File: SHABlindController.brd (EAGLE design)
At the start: 130.5 x 22 mm, 39 parts, among them IC1 SPARKCORE, IC2 HLKPM01, IC3 RXB1, Q1 2N7002, Q2 2N7002

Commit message: Added value to fuse
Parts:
- F1: value (none) -> 250V 3A
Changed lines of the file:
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@@
 <element name="PIEZO2" library="freetronics-jon" package="PIEZO12MMWIDEPOLARISED" value="PIEZOPOLARISED" x="23" y="11" rot="MR180"/>
 <element name="IC2" library="freetronics-jon" package="HLKPM01" value="HLKPM01" x="57" y="11" rot="MR0"/>
-<element name="F1" library="freetronics-jon" package="PICOFUSE" value="" x="62" y="8.5">
+<element name="F1" library="freetronics-jon" package="PICOFUSE" value="250V 3A" x="62" y="8.5">
 <attribute name="OC_NEWARK" value="unknown" x="62" y="8.5" size="1.778" layer="27" display="off"/>
 <attribute name="MPN" value="" x="62" y="8.5" size="1.778" layer="27" display="off"/>

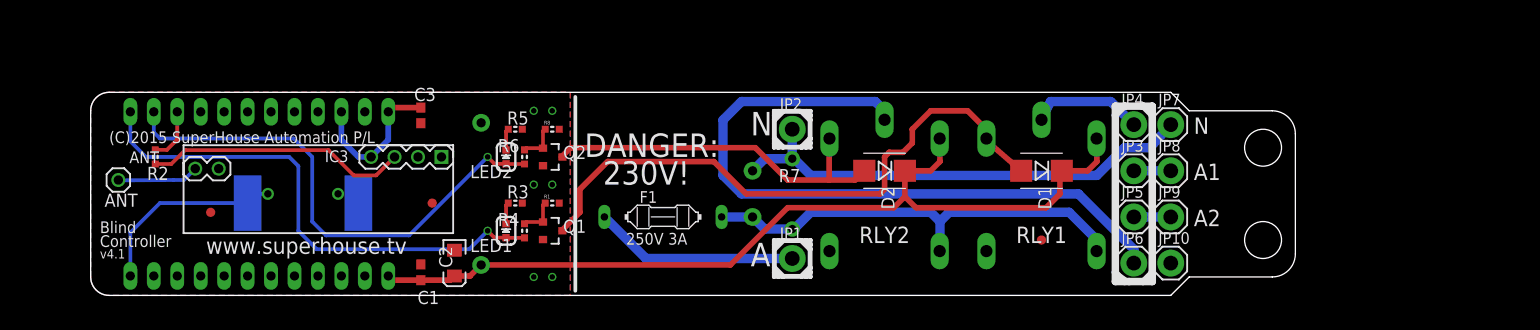
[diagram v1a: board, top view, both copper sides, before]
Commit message: Added solder-jumper to link GND and Neutral Reduced spacing between relays Increased length of fuse footprint
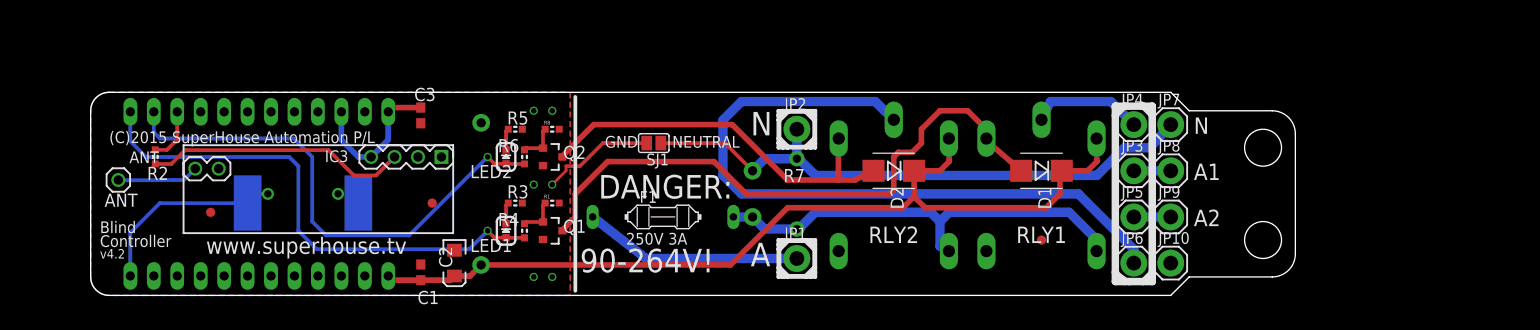
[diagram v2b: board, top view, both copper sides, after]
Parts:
- added SJ1: GND-NEUTRAL-LINK, freetronics-master-v1.1:SJ
- moved D2 1.00 mm to (87.0, 13.5)
- moved RLY2 1.00 mm to (87.0, 9.50)
- moved JP1 0.50 mm to (76.5, 4.00)
- moved JP2 0.50 mm to (76.5, 18.0)
- moved R7 0.50 mm to (76.5, 11.0)
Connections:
- net GND: now also SJ1.2
- net NEUTRAL: now also SJ1.1
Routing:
- net GND: track 0.00 -> 12.4 mm
- net NEUTRAL: track 52.4 -> 63.6 mm
- net N$3: track 40.7 -> 43.6 mm
- net N$9: track 22.2 -> 23.7 mm
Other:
- board text added: "90-264V!"
- board text added: "GND"
- board text added: "NEUTRAL"
- board text added: "v4.2"
- board text removed: "230V!"
- board text removed: "v4.1"

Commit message: Layout updates
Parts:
- removed JP10: EARTH, freetronics-master-v1.1:1X01LARGE
- removed JP3, JP8: ACTIVE1, freetronics-master-v1.1:1X01LARGE
- removed JP5, JP9: ACTIVE2, freetronics-master-v1.1:1X01LARGE
- added C4: 100nF 0603, freetronics-master-v1.1:0603
- added IC4: AH180-PL-A, freetronics-jon:TO92FLATUP
- added LED3: ROTATE/GREEN, freetronics:LED-0603
- added R10: 1K 0603, freetronics-master-v1:0603
- added R11, R9: 10K 0603, freetronics-master-v1:0603
- added R12: 10K, freetronics:0603
- added S2: 2P-JST-PTH, freetronics-jon:JST-2MM-TH-RA
- moved F1 73.5 mm to (135.5, 10.0), flipped to the bottom, turned to 90 degrees
- moved JP2 69.5 mm to (145.0, 6.00)
- moved JP1 69.2 mm to (145.0, 14.0)
- moved R7 63.0 mm to (139.5, 13.0)
- moved JP6 35.3 mm to (141.0, 25.0)
- moved JP4 33.6 mm to (146.0, 25.0)
- moved FID2 29.2 mm to (42.0, 12.0)
- moved C1 25.3 mm to (60.8, 6.50)
- moved C2 25.3 mm to (64.4, 7.50)
- moved C3 25.3 mm to (60.8, 23.5)
- moved FID3 25.3 mm to (62.0, 14.0)
- moved IC1 25.3 mm to (42.0, 15.0)
- moved IC2 25.3 mm to (82.0, 15.0)
- moved IC3 25.3 mm to (63.0, 19.0)
- moved LED1 25.3 mm to (70.0, 11.0)
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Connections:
- removed net D3: IC1.P$4
- removed net D4: IC1.P$5
- removed net D5: IC1.P$6
- removed net EARTH: JP10.1
- removed net N$7: JP3.1, JP8.1
- removed net N$8: JP5.1, JP9.1
- new net D3_BUTTON: IC1.P$4, R11.1, S2.POS
- new net D4_ROTATE: IC1.P$5, IC4.3, R10.2, R9.1
- new net D5_TYPE: IC1.P$6, R12.1
- new net N$11: LED3.C, R10.1
- net GND: now also C4.2, IC4.2, R12.2, S2.NEG
- net VCC: now also C4.1, IC4.1, LED3.A, R11.2, R9.2
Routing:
- net VCC: track 16.4 -> 99.5 mm
- net D4_ROTATE: track 0.00 -> 44.4 mm
- net N$17: track 75.5 -> 36.5 mm
- net D3_BUTTON: track 0.00 -> 28.3 mm
- net D5_TYPE: track 0.00 -> 18.8 mm
- net N$135: track 28.5 -> 47.1 mm
- net NEUTRAL: track 63.6 -> 77.6 mm
- net N$14: track 12.3 -> 25.9 mm
- net ACTIVE: track 48.8 -> 59.2 mm
- net N$3: track 43.6 -> 34.6 mm
- net N$1: track 8.86 -> 16.1 mm
- net N$9: track 23.7 -> 19.7 mm
- net N$8: track 4.00 -> 0.00 mm
- net N$7: track 4.00 -> 0.00 mm
- net GND: track 12.4 -> 9.65 mm
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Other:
- board size 130.5 x 22 mm -> 155 x 30 mm
- board text added: "+"
- board text added: "B"
- board text added: "BL"
- board text added: "BR"
- board text added: "BUTTON"
- board text added: "Blind Controller v5.0"
- board text added: "HALL"
- board text added: "R"
- board text added: "ROTATE"
- board text added: "W"
- board text removed: "2 x 330R 0603 3 x 1K 0603 2 x 10K 0603 2 x 1N4004 SMA 2 x 1uF 0603 1 x 10uF 6.3V TANT 2 x 2N7002 2 x GREEN LED"
- board text removed: "Blind"
- board text removed: "Controller"
- board text removed: "v4.2"
